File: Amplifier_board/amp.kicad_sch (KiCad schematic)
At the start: 31 parts, among them J12 Conn_01x03_Pin, J8 Conn_01x03_Pin, U4 TPA3111D1PWPR

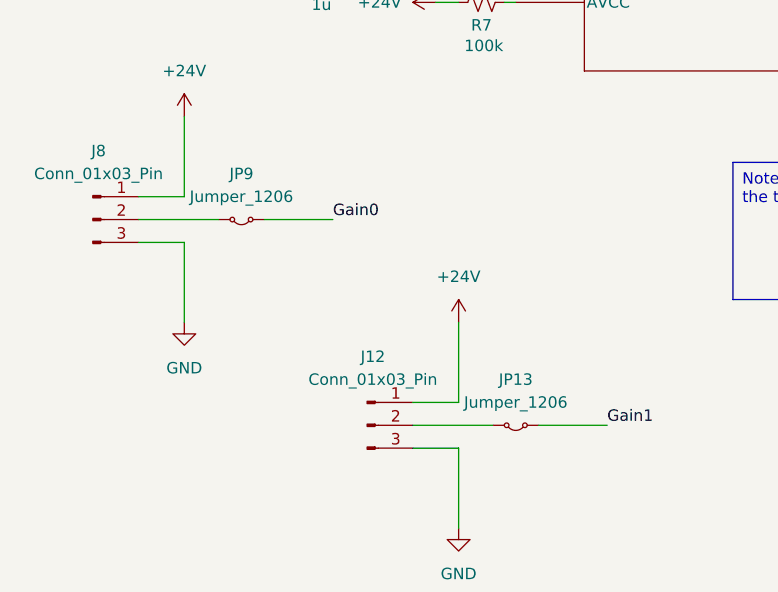
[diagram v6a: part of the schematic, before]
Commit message: Removed buffers on DAC board
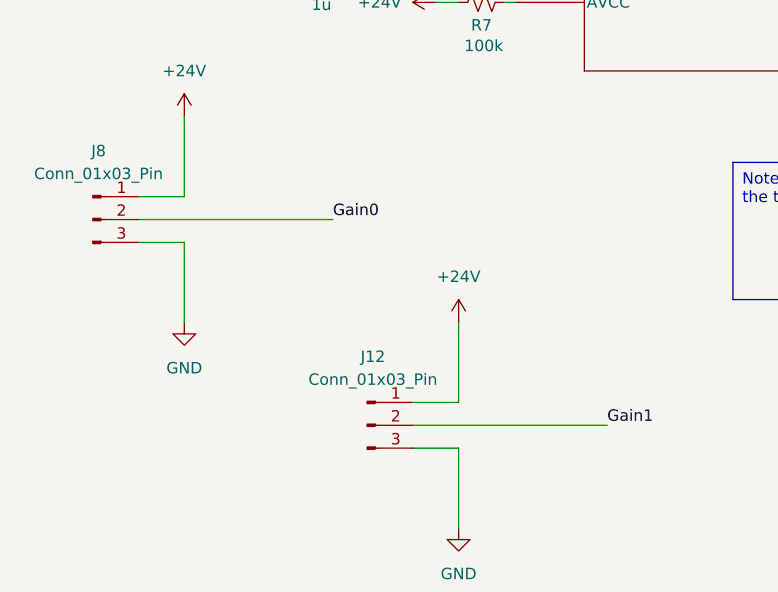
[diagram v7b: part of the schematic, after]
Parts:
- removed JP13, JP9: Jumper_1206, Resistor_SMD:R_1206_3216Metric_Pad1.30x1.75mm_HandSolder, symbol Jumper:Jumper_2_Small_Bridged
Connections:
- net Gain0: now also J8.2 (Pin_2)
- net Gain1: now also J12.2 (Pin_2)
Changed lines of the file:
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@@
 	(wire
 		(pts
-			(xy 60.96 120.65) (xy 69.85 120.65)
+			(xy 60.96 120.65) (xy 82.55 120.65)
 		)
 		(stroke
@@
 	(wire
 		(pts
-			(xy 91.44 143.51) (xy 100.33 143.51)
+			(xy 91.44 143.51) (xy 113.03 143.51)
 		)
 		(stroke
@@
 	(wire
 		(pts
-			(xy 74.93 120.65) (xy 82.55 120.65)
-		)
-		(stroke
-			(width 0)
-			(type default)
-		)
-	)
-	(wire
-		(pts
 			(xy 100.33 68.58) (xy 100.33 71.12)
 		)
@@
 	(wire
 		(pts
-			(xy 105.41 143.51) (xy 113.03 143.51)
-		)
-		(stroke
-			(width 0)
-			(type default)
-		)
-	)
-	(wire
-		(pts
 			(xy 168.91 63.5) (xy 171.45 63.5)
 		)
@@
 					(unit 1)
 				)
-			)
-		)
-	)
-	(symbol
-		(lib_id "Jumper:Jumper_2_Small_Bridged")
-		(at 102.87 143.51 180)
-		(unit 1)
-		(exclude_from_sim yes)
-		(in_bom yes)
-		(on_board yes)
-		(dnp no)
-		(fields_autoplaced yes)
-		(property "Reference" "JP13"
-			(at 102.87 138.43 0)
-			(effects
-				(font
-					(size 1.27 1.27)
-				)
-			)
-		)
-		(property "Value" "Jumper_1206"
-			(at 102.87 140.97 0)
-			(effects
-				(font
-					(size 1.27 1.27)
-				)
-			)
-		)
-		(property "Footprint" "Resistor_SMD:R_1206_3216Metric_Pad1.30x1.75mm_HandSolder"
-			(at 102.87 143.51 0)
-			(effects
-				(font
-					(size 1.27 1.27)
-				)
-				(hide yes)
-			)
-		)
-		(property "Datasheet" "~"
-			(at 102.87 143.51 0)
-			(effects
-				(font
-					(size 1.27 1.27)
-				)
-				(hide yes)
-			)
-		)
-		(property "Description" "Jumper, 2-pole, small symbol, bridged"
-			(at 102.87 143.51 0)
-			(effects
-				(font
-					(size 1.27 1.27)
-				)
-				(hide yes)
-			)
-		)
-		(pin "2"
-		)
-		(pin "1"
-		)
-		(instances
-			(project "Amplifier_board"
-				(path "/991395a4-3885-4774-b551-0bfe029123d3/1a21d9eb-2329-48b7-8877-ba841ad5b065"
-					(reference "JP16")
-					(unit 1)
-				)
-				(path "/991395a4-3885-4774-b551-0bfe029123d3/26541e86-2f42-461f-bb67-92277cc28a80"
-					(reference "JP13")
-					(unit 1)
-				)
-				(path "/991395a4-3885-4774-b551-0bfe029123d3/e8898fe0-55dc-4973-83e9-f265cc01a132"
-					(reference "JP15")
-					(unit 1)
-				)
-				(path "/991395a4-3885-4774-b551-0bfe029123d3/eadc8ba5-6d36-4b46-a20f-2896249de991"
-					(reference "JP14")
-					(unit 1)
-				)
-			)
-		)
-	)
-	(symbol
-		(lib_id "Jumper:Jumper_2_Small_Bridged")
-		(at 72.39 120.65 180)
-		(unit 1)
-		(exclude_from_sim yes)
-		(in_bom yes)
-		(on_board yes)
-		(dnp no)
-		(fields_autoplaced yes)
-		(property "Reference" "JP9"
-			(at 72.39 115.57 0)
-			(effects
-				(font
-					(size 1.27 1.27)
-				)
-			)
-		)
-		(property "Value" "Jumper_1206"
-			(at 72.39 118.11 0)
-			(effects
-				(font
-					(size 1.27 1.27)
-				)
-			)
-		)
-		(property "Footprint" "Resistor_SMD:R_1206_3216Metric_Pad1.30x1.75mm_HandSolder"
-			(at 72.39 120.65 0)
-			(effects
-				(font
-					(size 1.27 1.27)
-				)
-				(hide yes)
-			)
-		)
-		(property "Datasheet" "~"
-			(at 72.39 120.65 0)
-			(effects
-				(font
-					(size 1.27 1.27)
-				)
-				(hide yes)
-			)
-		)
-		(property "Description" "Jumper, 2-pole, small symbol, bridged"
-			(at 72.39 120.65 0)
-			(effects
-				(font
-					(size 1.27 1.27)
-				)
-				(hide yes)
-			)
-		)
-		(pin "2"
-		)
-		(pin "1"
-		)
-		(instances
-			(project "Amplifier_board"
-				(path "/991395a4-3885-4774-b551-0bfe029123d3/1a21d9eb-2329-48b7-8877-ba841ad5b065"
-					(reference "JP12")
-					(unit 1)
-				)
-				(path "/991395a4-3885-4774-b551-0bfe029123d3/26541e86-2f42-461f-bb67-92277cc28a80"
-					(reference "JP9")
-					(unit 1)
-				)
-				(path "/991395a4-3885-4774-b551-0bfe029123d3/e8898fe0-55dc-4973-83e9-f265cc01a132"
-					(reference "JP11")
-					(unit 1)
-				)
-				(path "/991395a4-3885-4774-b551-0bfe029123d3/eadc8ba5-6d36-4b46-a20f-2896249de991"
-					(reference "JP10")
-					(unit 1)
-				)

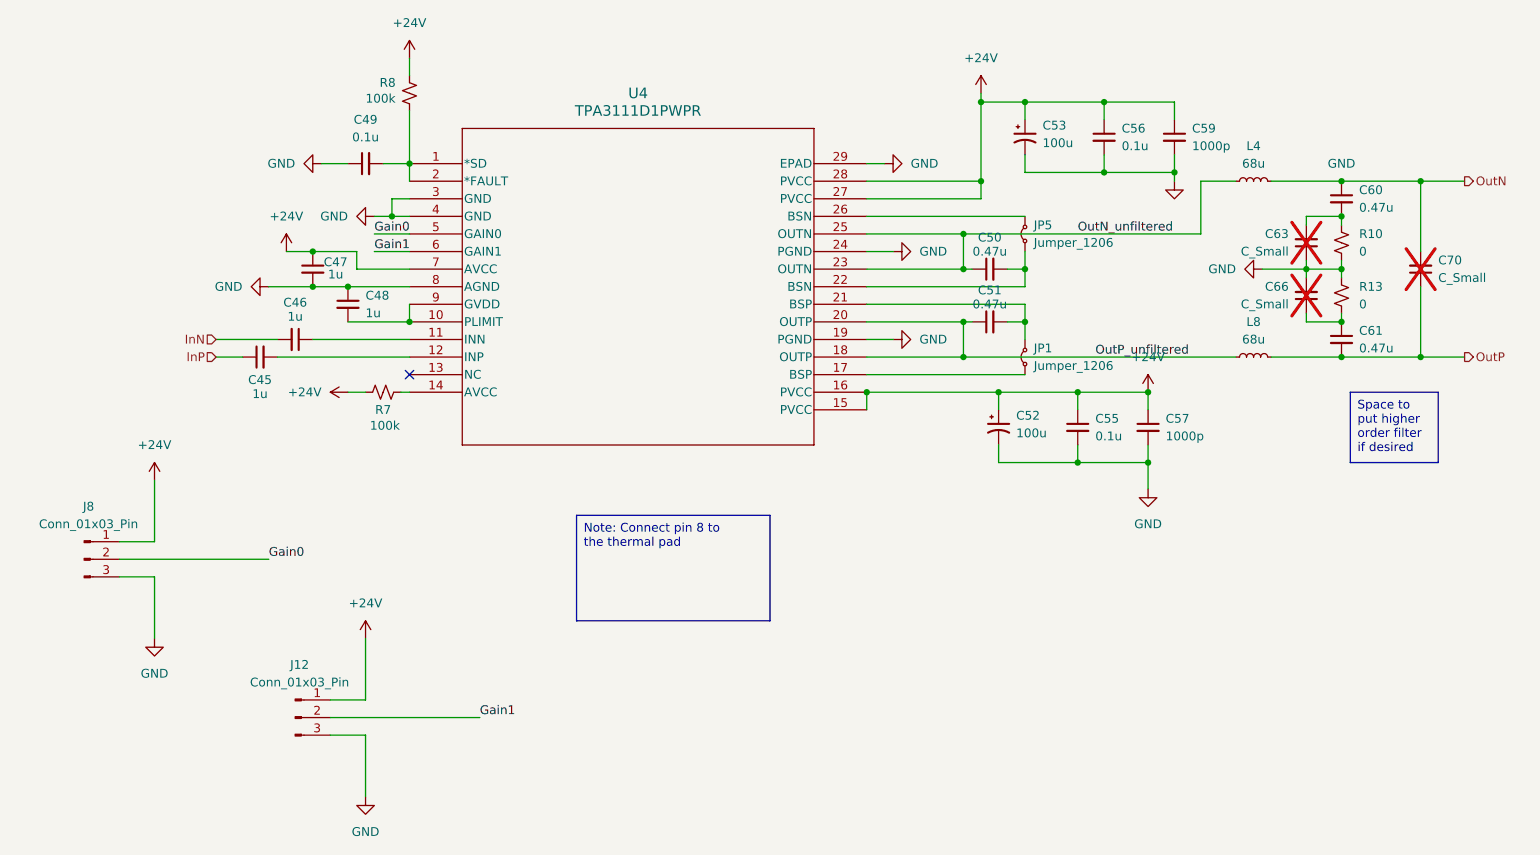
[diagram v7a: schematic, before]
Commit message: Added test points, almost finished layout for amp board
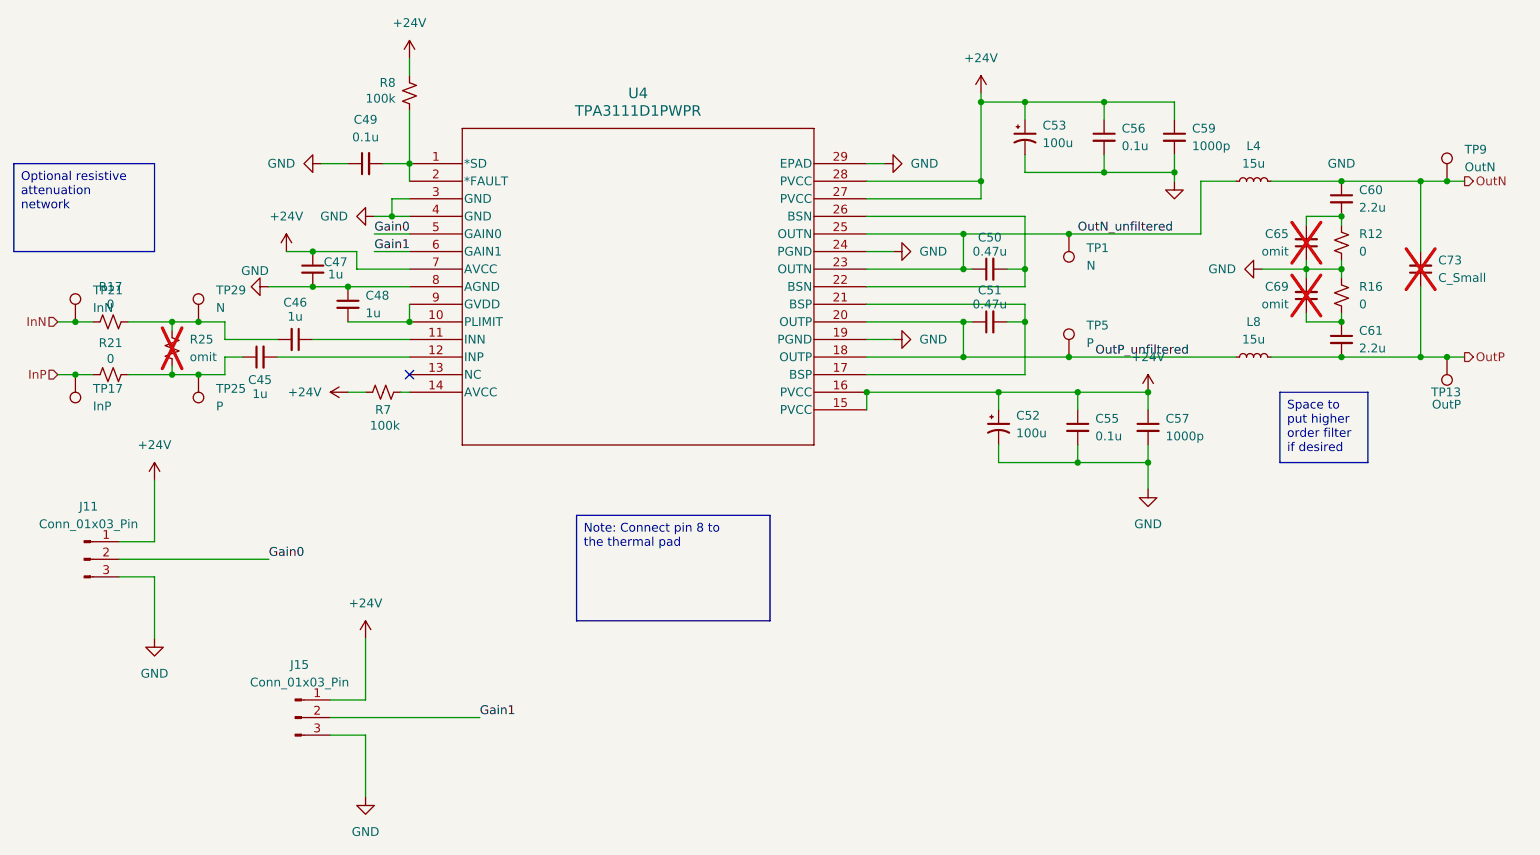
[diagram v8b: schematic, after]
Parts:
- removed JP1, JP5: Jumper_1206, Resistor_SMD:R_1206_3216Metric_Pad1.30x1.75mm_HandSolder, symbol Jumper:Jumper_2_Small_Bridged
- added R17, R21: 0, Resistor_SMD:R_0805_2012Metric_Pad1.20x1.40mm_HandSolder, symbol Device:R_Small_US
- added R25: omit, Resistor_SMD:R_0805_2012Metric_Pad1.20x1.40mm_HandSolder, symbol Device:R_Small_US
- added TP1, TP29: N, project_lib:TP_RCUCTE, symbol Connector:TestPoint
- added TP13: OutP, project_lib:TP_RCUCTE, symbol Connector:TestPoint
- added TP17: InP, project_lib:TP_RCUCTE, symbol Connector:TestPoint
- added TP21: InN, project_lib:TP_RCUCTE, symbol Connector:TestPoint
- added TP25, TP5: P, project_lib:TP_RCUCTE, symbol Connector:TestPoint
- added TP9: OutN, project_lib:TP_RCUCTE, symbol Connector:TestPoint
- C52, C53: footprint project_lib:WCAP-ASLI_6.3X7.7_DXL_ -> Capacitor_THT:CP_Radial_D6.3mm_P2.50mm
- C60, C61: value 0.47u -> 2.2u
- C65: renamed from C63; value C_Small -> omit
- C69: renamed from C66; value C_Small -> omit
- L4, L8: value 68u -> 15u; footprint Inductor_SMD:L_Taiyo-Yuden_NR-80xx_HandSoldering -> Inductor_SMD:L_Taiyo-Yuden_NR-50xx_HandSoldering
- U4: footprint PWP28_6P17X2P4 -> project_lib:PWP28_6P17X2P4
- renumbered C70 to C73, J8 to J11, J12 to J15, R10 to R12, R13 to R16
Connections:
- net InN: now also R17.2, TP21.1; no longer C46.2
- net InP: now also R21.2, TP17.1; no longer C45.1
- net OutN: now also TP9.1
- net OutN_unfiltered: now also TP1.1
- net OutP: now also TP13.1
- net OutP_unfiltered: now also TP5.1
- net at U4.17 (BSP): now also C51.2, U4.21 (BSP)
- net at C50.2, U4.22 (BSN): now also U4.26 (BSN)
- new net: C46.2, R17.1, R25.1, TP29.1
- new net: C45.1, R21.1, R25.2, TP25.1
